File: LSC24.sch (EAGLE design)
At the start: 123 parts, among them IC1 MCP23017SO, IC2 MCP23017SO, IC3 MCP23017SO, IC4 MCP23017SO, IC5 MCP23017SO, IC6 MCP23017SO, J1 RJ45-X8, J2 RJ45-X8, J3 RJ45-X8, J5 M06-PIN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

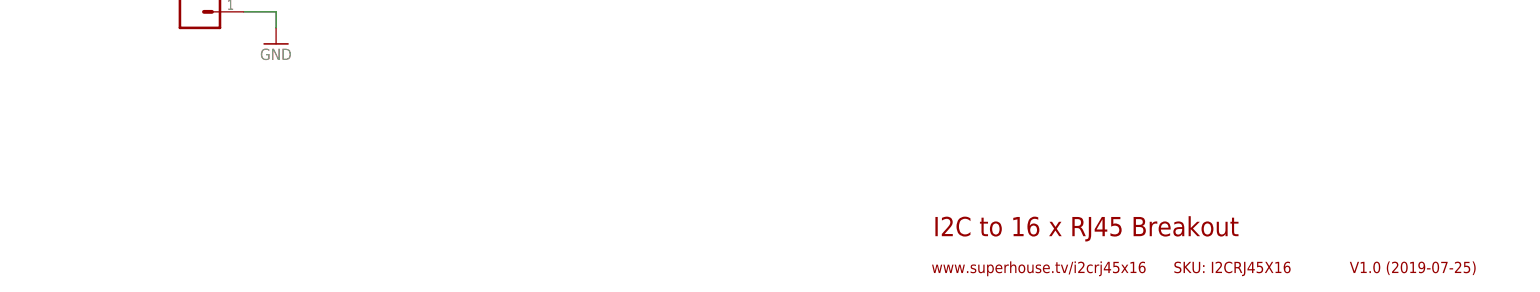
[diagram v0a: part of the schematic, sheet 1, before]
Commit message: Routing and silkscreen for Ethernet pass-through and external power
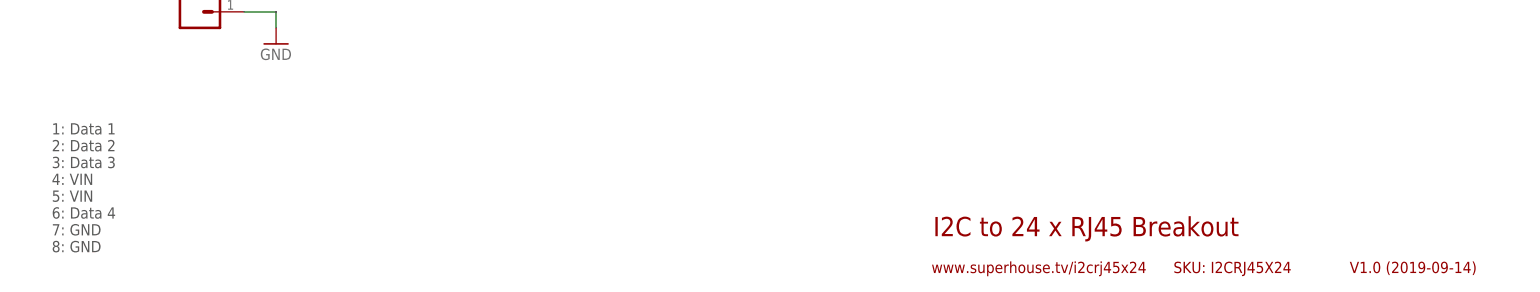
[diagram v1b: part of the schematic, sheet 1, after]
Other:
- note added: "1: Data 1 2: Data 2 3: Data 3 4: VIN 5: VIN 6: Data 4 7: GND 8: GND"
- note added: "I2C to 24 x RJ45 Breakout"
- note added: "SKU: I2CRJ45X24"
- note added: "V1.0 (2019-09-14)"
- note added: "www.superhouse.tv/i2crj45x24"
- note removed: "I2C to 16 x RJ45 Breakout"
- note removed: "SKU: I2CRJ45X16"
- note removed: "V1.0 (2019-07-25)"
- note removed: "www.superhouse.tv/i2crj45x16"
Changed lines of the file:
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@@
 <plain>
 <frame x1="0" y1="0" x2="248.92" y2="185.42" columns="8" rows="5" layer="94"/>
-<text x="149.86" y="12.7" size="3.048" layer="94">I2C to 16 x RJ45 Breakout</text>
-<text x="215.9" y="6.858" size="1.778" layer="94">V1.0 (2019-07-25)</text>
-<text x="149.606" y="6.858" size="1.778" layer="94">www.superhouse.tv/i2crj45x16</text>
-<text x="187.96" y="6.858" size="1.778" layer="94">SKU: I2CRJ45X16</text>
+<text x="149.86" y="12.7" size="3.048" layer="94">I2C to 24 x RJ45 Breakout</text>
+<text x="215.9" y="6.858" size="1.778" layer="94">V1.0 (2019-09-14)</text>
+<text x="149.606" y="6.858" size="1.778" layer="94">www.superhouse.tv/i2crj45x24</text>
+<text x="187.96" y="6.858" size="1.778" layer="94">SKU: I2CRJ45X24</text>
 <frame x1="147.32" y1="5.08" x2="243.84" y2="17.78" columns="0" rows="0" layer="94" border-left="no" border-top="no" border-right="no" border-bottom="no"/>
 <frame x1="185.42" y1="5.08" x2="213.36" y2="10.16" columns="8" rows="5" layer="94"/>
 <frame x1="213.36" y1="5.08" x2="243.84" y2="10.16" columns="8" rows="5" layer="94"/>
+<text x="10.16" y="10.16" size="1.778" layer="97">1: Data 1
+2: Data 2
+3: Data 3
+4: VIN
+5: VIN
+6: Data 4
+7: GND
+8: GND</text>
 </plain>
 <instances>
